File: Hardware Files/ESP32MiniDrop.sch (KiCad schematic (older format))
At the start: 31 parts, among them J2 Barrel_Jack, J3 AudioJack3, J4 Solenoid1 Terminal, J5 0.100\" 2x4 Header, M1 Conn_01x01, M2 Conn_01x01, M3 Conn_01x01, M4 Conn_01x01, Q3 NMOS 60V 46A, SW1 SPST (RED), SW2 SPST (BLUE), U2 AZ1117-3.3, U3 ESP32-WROOM-32, U4 4N25, U5 4N25

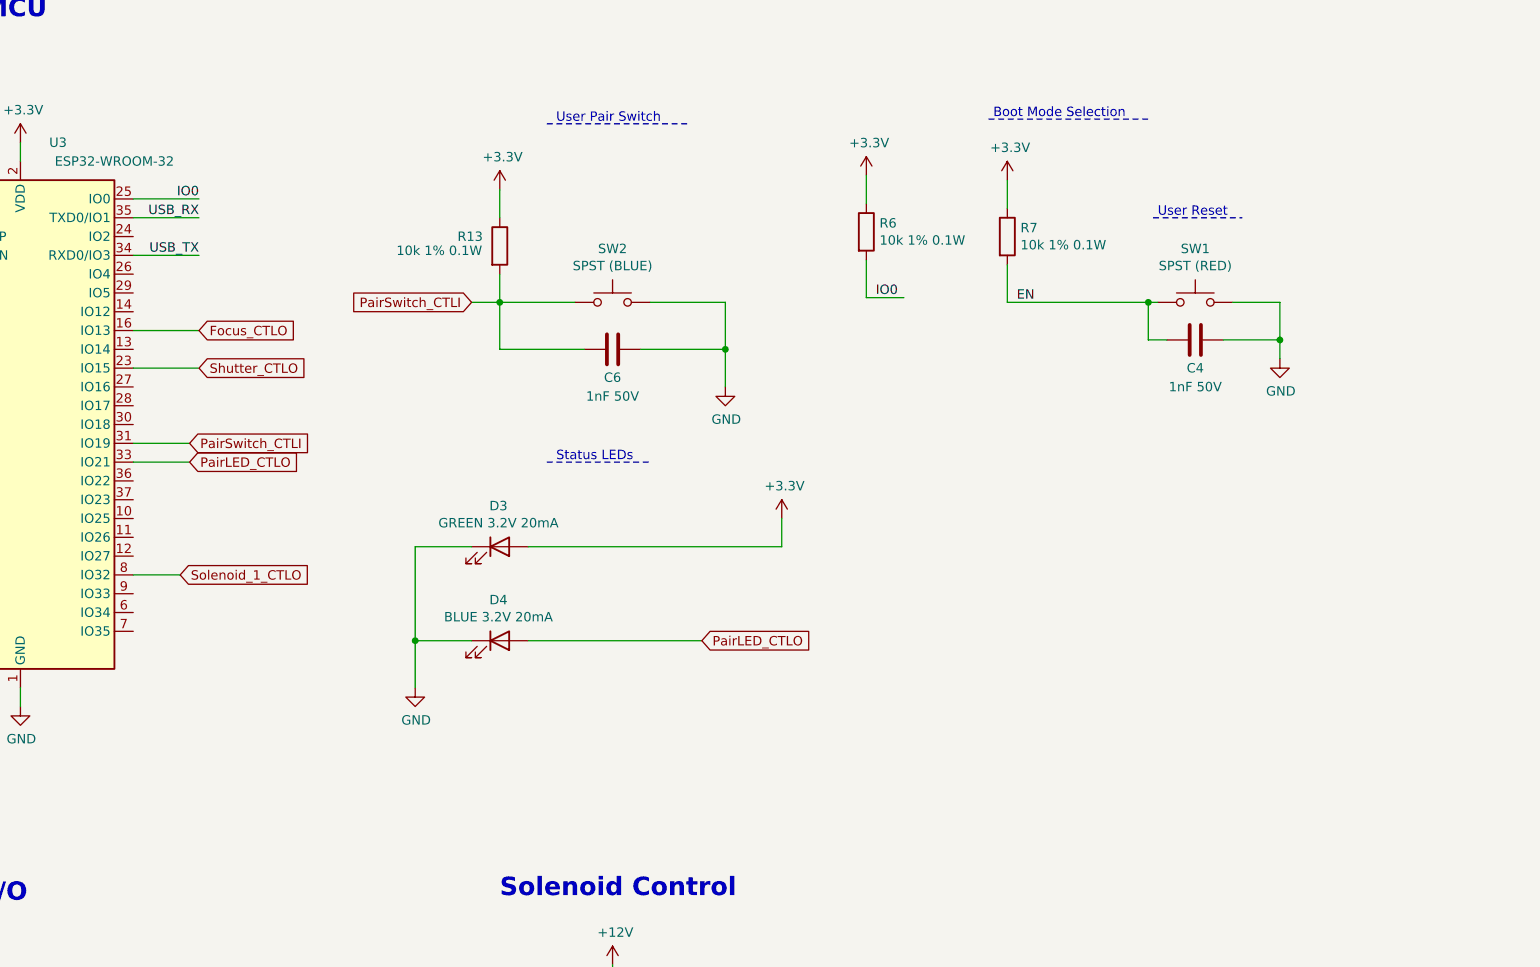
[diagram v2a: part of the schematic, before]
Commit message: Attach Pair Switch to ESP32 IO0 for boot mode selection
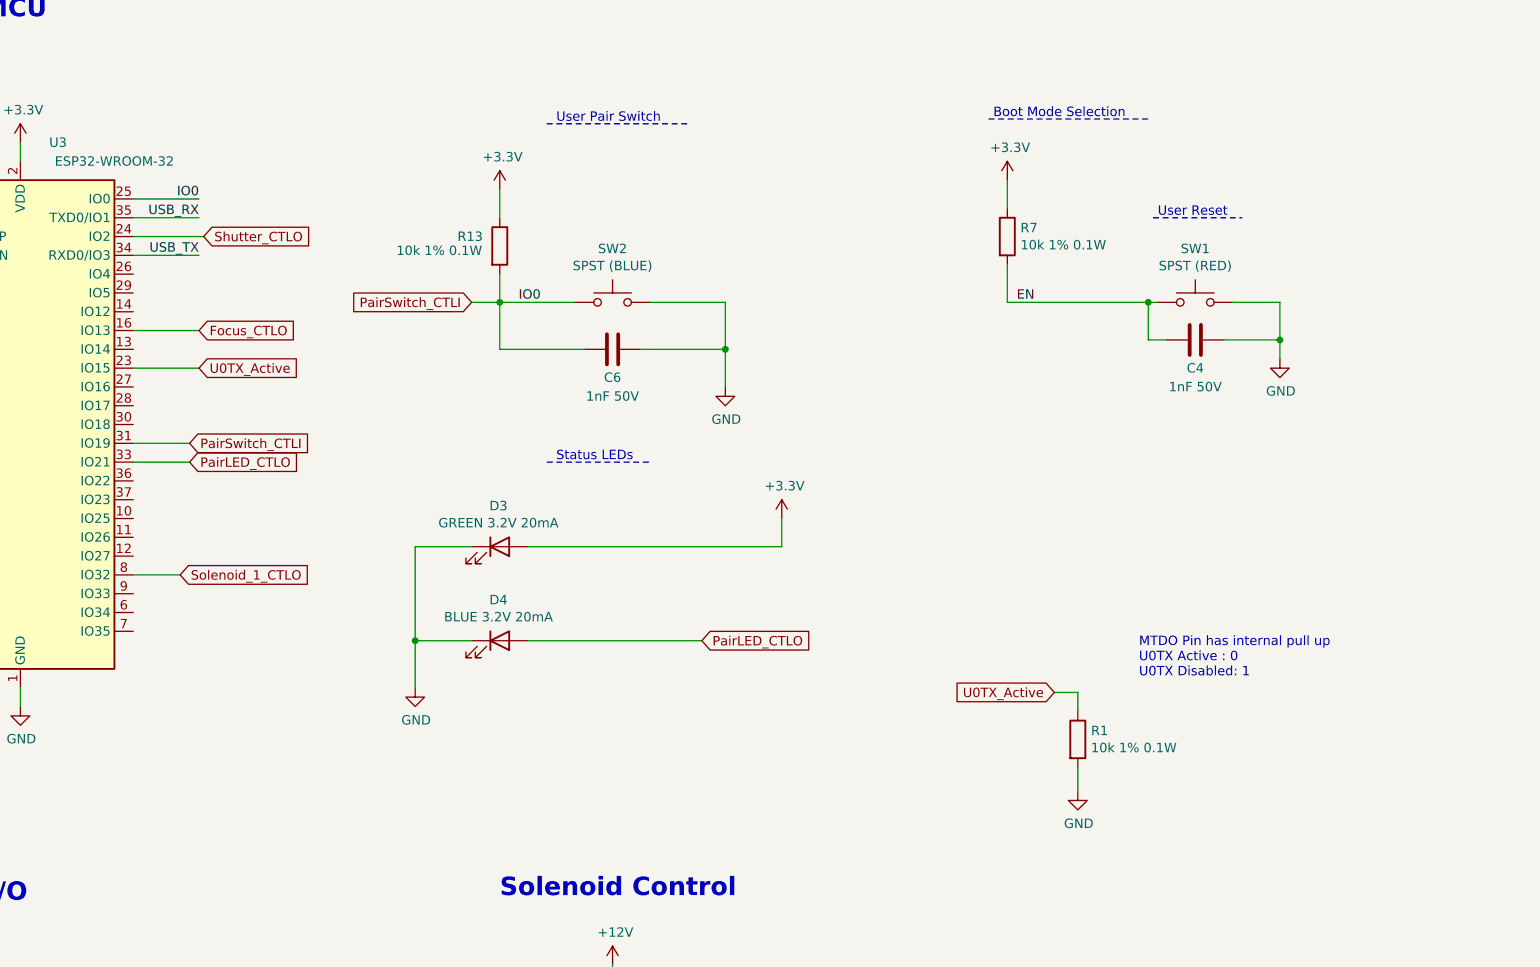
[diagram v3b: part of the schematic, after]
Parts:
- removed R6: 10k 1% 0.1W, Resistor_SMD:R_1206_3216Metric_Pad1.42x1.75mm_HandSolder, symbol Device:R
- added R1: 10k 1% 0.1W, Resistor_SMD:R_1206_3216Metric_Pad1.42x1.75mm_HandSolder, symbol Device:R
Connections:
- net IO0 is gone; now on net PairSwitch_CTLI: J5.4 (Pin_4), U3.25 (IO0)
- net GND: now also R1.2
- net Shutter_CTLO: now also U3.24 (IO2); no longer U3.23 (IO15)
- new net U0TX_Active: R1.1, U3.23 (IO15)
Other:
- note added: "MTDO Pin has internal pull up\nU0TX Active : 0\nU0TX Disabled: 1"
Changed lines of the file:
@@
-$Comp
-L Device:R R?
-U 1 1 5F512BE2
-P 7675 2050
-AR Path="/5F45F2B5/5F512BE2" Ref="R?"  Part="1"
-AR Path="/5F512BE2" Ref="R6"  Part="1"
-F 0 "R6" H 7745 2096 50  0000 L CNN
-F 1 "10k 1% 0.1W" H 7745 2005 50  0000 L CNN
-F 2 "Resistor_SMD:R_1206_3216Metric_Pad1.42x1.75mm_HandSolder" V 7605 2050 50  0001 C CNN
-F 3 "~" H 7675 2050 50  0001 C CNN
-F 4 "Yageo" H 7675 2050 50  0001 C CNN "MF"
-F 5 "" H 7675 2050 50  0001 C CNN "MPN"
-	1    7675 2050
-	1    0    0    -1
-$EndComp
-Wire Wire Line
-	7675 2200 7675 2400
-Text Label 7725 2400 0    50   ~ 0
-IO0
-$Comp
-L power:+3.3V #PWR?
-U 1 1 5F512BEA
-P 7675 1750
-AR Path="/5F45F2B5/5F512BEA" Ref="#PWR?"  Part="1"
-AR Path="/5F512BEA" Ref="#PWR010"  Part="1"
-F 0 "#PWR010" H 7675 1600 50  0001 C CNN
-F 1 "+3.3V" H 7690 1923 50  0000 C CNN
-F 2 "" H 7675 1750 50  0001 C CNN
-F 3 "" H 7675 1750 50  0001 C CNN
-	1    7675 1750
-	1    0    0    -1
-$EndComp
-Wire Wire Line
-	7675 1750 7675 1900
 $Comp
 L Device:R R?
@@
 Wire Wire Line
 	2950 9925 2950 10000
-Wire Wire Line
-	7675 2400 7875 2400
 Text Notes 3475 9075 0    50   ~ 0
 Regulator for both 12V and 5V\ninput sources
@@
 	4125 2575 3775 2575
 Wire Wire Line
-	4125 2775 3775 2775
-Wire Wire Line
 	8425 2425 9175 2425
 $Comp
@@
 	1275 4075 1275 3975
 Connection ~ 1275 3975
-Text GLabel 4125 2775 2    50   Input ~ 0
+Text GLabel 4150 2075 2    50   Input ~ 0
 Shutter_CTLO
 Text GLabel 4125 2575 2    50   Input ~ 0
@@
 Wire Wire Line
 	5875 4225 6800 4225
+$Comp
+L Device:R R?
+U 1 1 5F72D7F7
+P 8800 4750
+AR Path="/5F45F2B5/5F72D7F7" Ref="R?"  Part="1"
+AR Path="/5F72D7F7" Ref="R1"  Part="1"
+F 0 "R1" H 8870 4796 50  0000 L CNN
+F 1 "10k 1% 0.1W" H 8870 4705 50  0000 L CNN
+F 2 "Resistor_SMD:R_1206_3216Metric_Pad1.42x1.75mm_HandSolder" V 8730 4750 50  0001 C CNN
+F 3 "~" H 8800 4750 50  0001 C CNN
+F 4 "Yageo" H 8800 4750 50  0001 C CNN "MF"
+F 5 "" H 8800 4750 50  0001 C CNN "MPN"
+	1    8800 4750
+	1    0    0    -1
+$EndComp
+Text GLabel 4125 2775 2    50   Input ~ 0
+U0TX_Active
+Wire Wire Line
+	4150 2075 3775 2075
+Wire Wire Line
+	4125 2775 3775 2775
+Text GLabel 8675 4500 0    50   Input ~ 0
+U0TX_Active
+Wire Wire Line
+	8675 4500 8800 4500
+Wire Wire Line
+	8800 4500 8800 4600
+$Comp
+L power:GND #PWR?
+U 1 1 5F750570
+P 8800 5025
+AR Path="/5F45F2B5/5F750570" Ref="#PWR?"  Part="1"
+AR Path="/5F750570" Ref="#PWR0103"  Part="1"
+F 0 "#PWR0103" H 8800 4775 50  0001 C CNN
+F 1 "GND" H 8805 4852 50  0000 C CNN
+F 2 "" H 8800 5025 50  0001 C CNN
+F 3 "" H 8800 5025 50  0001 C CNN
+	1    8800 5025
+	1    0    0    -1
+$EndComp
+Wire Wire Line
+	8800 4900 8800 5025
+Text Notes 9125 4425 0    50   ~ 0
+MTDO Pin has internal pull up\nU0TX Active : 0\nU0TX Disabled: 1
+Text Label 5825 2425 0    50   ~ 0
+IO0
 $EndSCHEMATC

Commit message: Update Component MPN and Values
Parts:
- removed C9: 22uF 6.3V, Capacitor_SMD:C_1206_3216Metric_Pad1.42x1.75mm_HandSolder, symbol Device:C
- C1: renamed from C4; MF (none) -> Walsin Technology Corporation; MPN (none) -> 1206B102K500CT
- C2: renamed from C5; value 10uF 50V -> 10uF 25V 10%; MPN CL31A106MBHNNNE -> CL31A106MAHNNNE
- C3: renamed from C8; MF (none) -> Samsung Electro-Mechanics; MPN (none) -> CL31B105KBHNFNE
- C4: renamed from C6; MF (none) -> Walsin Technology Corporation; MPN (none) -> 1206B102K500CT
- C5: renamed from C7; value 10uF 50V -> 10uF 25V 10%; MPN CL31A106MBHNNNE -> CL31A106MAHNNNE
- R1: renamed from R7; value 10k 1% 0.1W -> 10k 5% 0.25W; MPN (none) -> RC1206JR-0710KL
- R2: renamed from R13; value 10k 1% 0.1W -> 10k 5% 0.25W; MPN (none) -> RC1206JR-0710KL
- R3: renamed from R1; value 10k 1% 0.1W -> 10k 5% 0.25W; MPN (none) -> RC1206JR-0710KL
- R4: renamed from R14; value 220R 1% 0.1W -> 220R 5% 0.25W; MPN (none) -> RC1206JR-07220RL
- R5: renamed from R16; value 10k 1% 0.1W -> 10k 5% 0.25W; MPN (none) -> RC1206JR-0710KL
- R6: renamed from R15; value 220R 1% 0.1W -> 220R 5% 0.25W; MPN (none) -> RC1206JR-07220RL
- renumbered D3 to D1, D4 to D2, D7 to D3, D6 to D4, J5 to J1, J4 to J2, J2 to J4, Q3 to Q1, SW2 to SW1, SW1 to SW2, U3 to U1, U4 to U2, U5 to U3, U2 to U4
